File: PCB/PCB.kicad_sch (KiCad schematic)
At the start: 6 parts, among them SW10 SW2_Push, SW11 SW3_Push, SW4 RotaryEncoder_Switch, SW9 SW1_Push, U4 ER_OLEDM0.91_1x-I2C, U5 MOUDLE-SEEEDUINO-XIAO

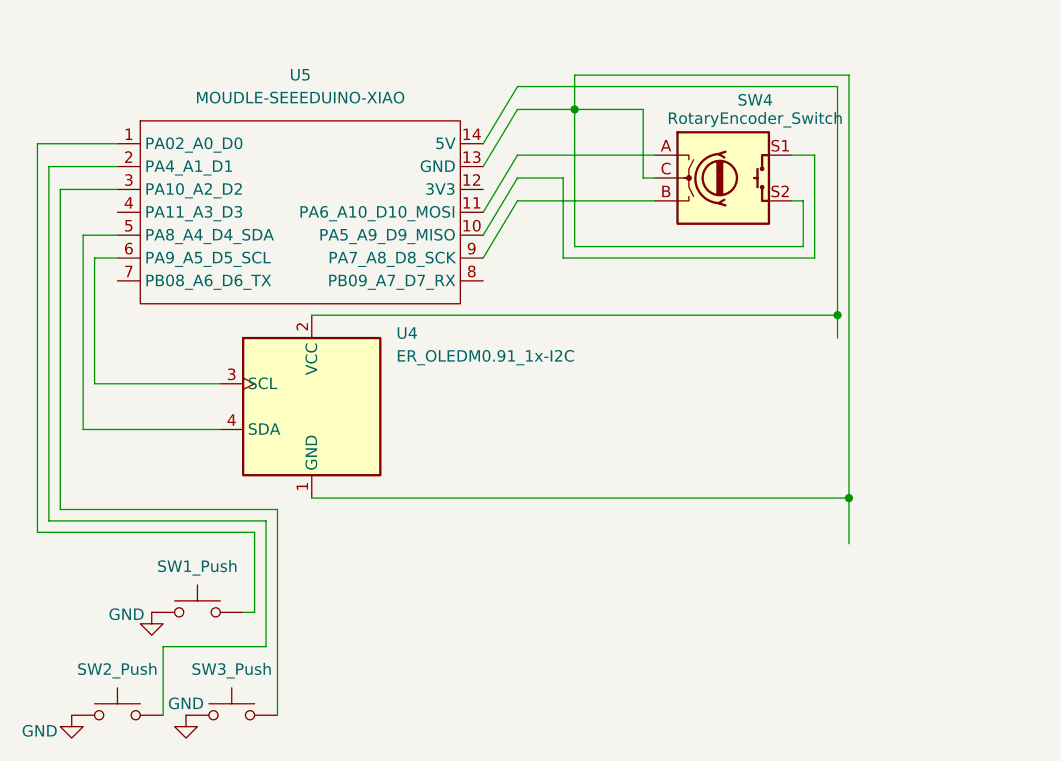
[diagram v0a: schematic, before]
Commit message: Add Hakin Pad schematic image
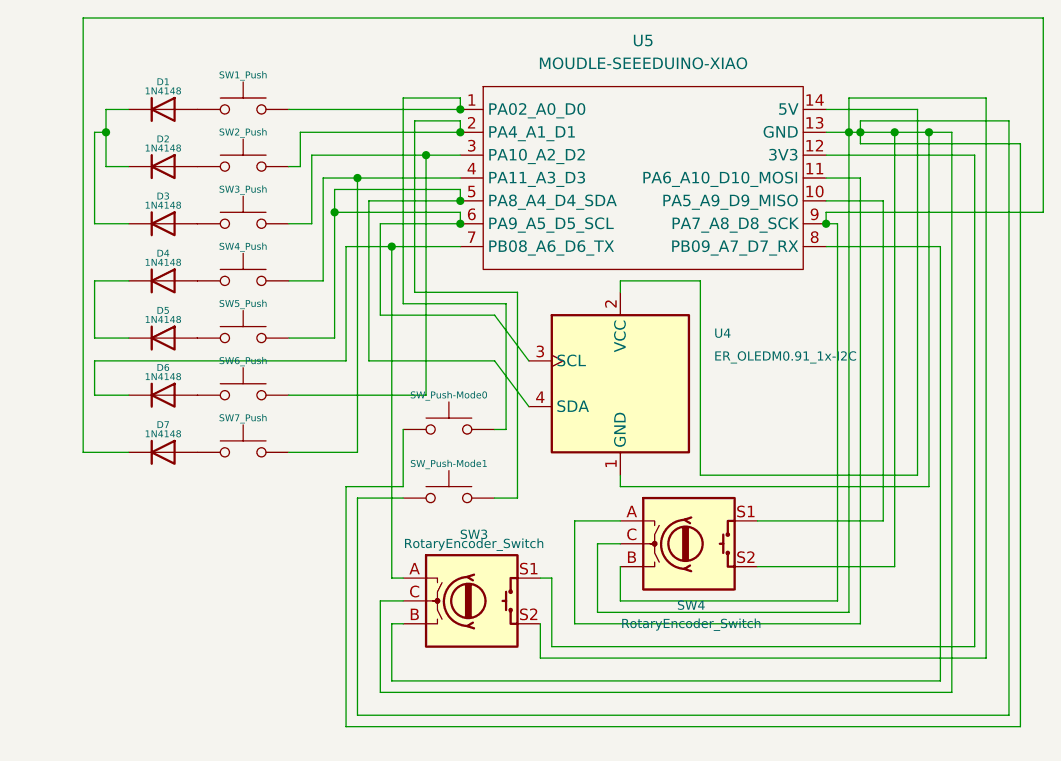
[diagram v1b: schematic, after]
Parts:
- added D1, D2, D3, D4, D5, D6, D7: 1N4148, Diode_THT:D_DO-35_SOD27_P7.62mm_Horizontal, symbol Diode:1N4148
- added SW1: SW4_Push, Button_Switch_SMD:Nidec_Copal_CAS-120A, symbol Switch:SW_Push
- added SW2: SW5_Push, symbol Switch:SW_Push
- added SW3: RotaryEncoder_Switch, symbol Device:RotaryEncoder_Switch
- added SW5: SW6_Push, Button_Switch_THT:SW_NKK_GW12LJP, symbol Switch:SW_Push
- added SW6: SW7_Push, symbol Switch:SW_Push
- added SW7: SW_Push-Mode0, Button_Switch_THT:SW_NKK_GW12LJP, symbol Switch:SW_Push
- added SW8: SW_Push-Mode1, symbol Switch:SW_Push
- SW10, SW11: footprint (none) -> Button_Switch_Keyboard:SW_Cherry_MX_1.00u_PCB
- SW4: footprint (none) -> Rotary_Encoder:RotaryEncoder_Alps_EC11E-Switch_Vertical_H20mm
- SW9: footprint Button_Switch_THT:SW_NKK_GW12LJP -> Button_Switch_Keyboard:SW_Cherry_MX_1.00u_PCB
- U5: footprint Package_BGA:XFBGA-36_3.5x3.5mm_Layout6x6_P0.5mm -> footprints:XIAO-Generic-Hybrid-14P-2.54-21X17.8MM
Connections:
- net at SW11.2, U5.3 (PA10_A2_D2): now also SW5.2
- net at SW9.2, U5.1 (PA02_A0_D0): now also SW7.2
- net at U5.12 (3V3): now also SW3.S1
- net at SW4.C, SW4.S2, U4.1 (GND)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: now also SW3.C, SW3.S2, SW7.1, SW8.1
- net at SW10.2, U5.2 (PA4_A1_D1): now also SW8.2
- net at U5.4 (PA11_A3_D3): now also SW1.2, SW6.2
- net at U4.4 (SDA), U5.5 (PA8_A4_D4_SDA): now also U4.3 (SCL), U5.6 (PA9_A5_D5_SCL), SW2.2
- net at U5.7 (PB08_A6_D6_TX): now also D6.1 (K), SW3.A
- net at U5.8 (PB09_A7_D7_RX): now also SW3.B
- net at SW4.B, U5.9 (PA7_A8_D8_SCK): now also D7.1 (K)
- removed net GND: SW10.1, SW11.1, SW9.1
- new net: D1.1 (K), D2.1 (K), D3.1 (K)
- new net: D2.2 (A), SW10.1
- new net: D3.2 (A), SW11.1
- new net: D7.2 (A), SW6.1
- new net: D5.2 (A), SW2.1
- new net: D4.1 (K), D5.1 (K)
- new net: D4.2 (A), SW1.1
- new net: D1.2 (A), SW9.1
- new net: D6.2 (A), SW5.1
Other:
- moved on the sheet: SW4, U4, U5
